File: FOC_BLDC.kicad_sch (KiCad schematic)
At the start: 0 parts

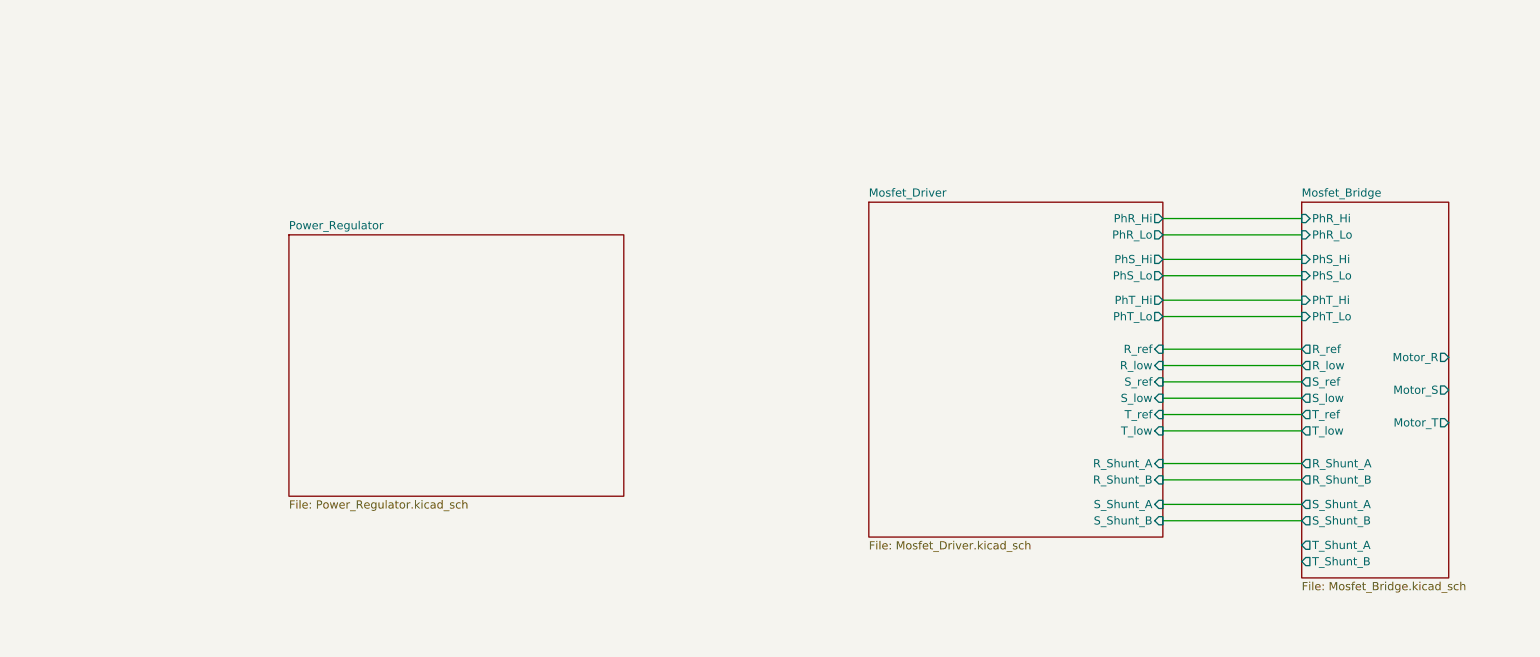
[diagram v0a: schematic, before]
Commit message: Finished basic schematic.
Need to add inline opamps and footprints to all components.
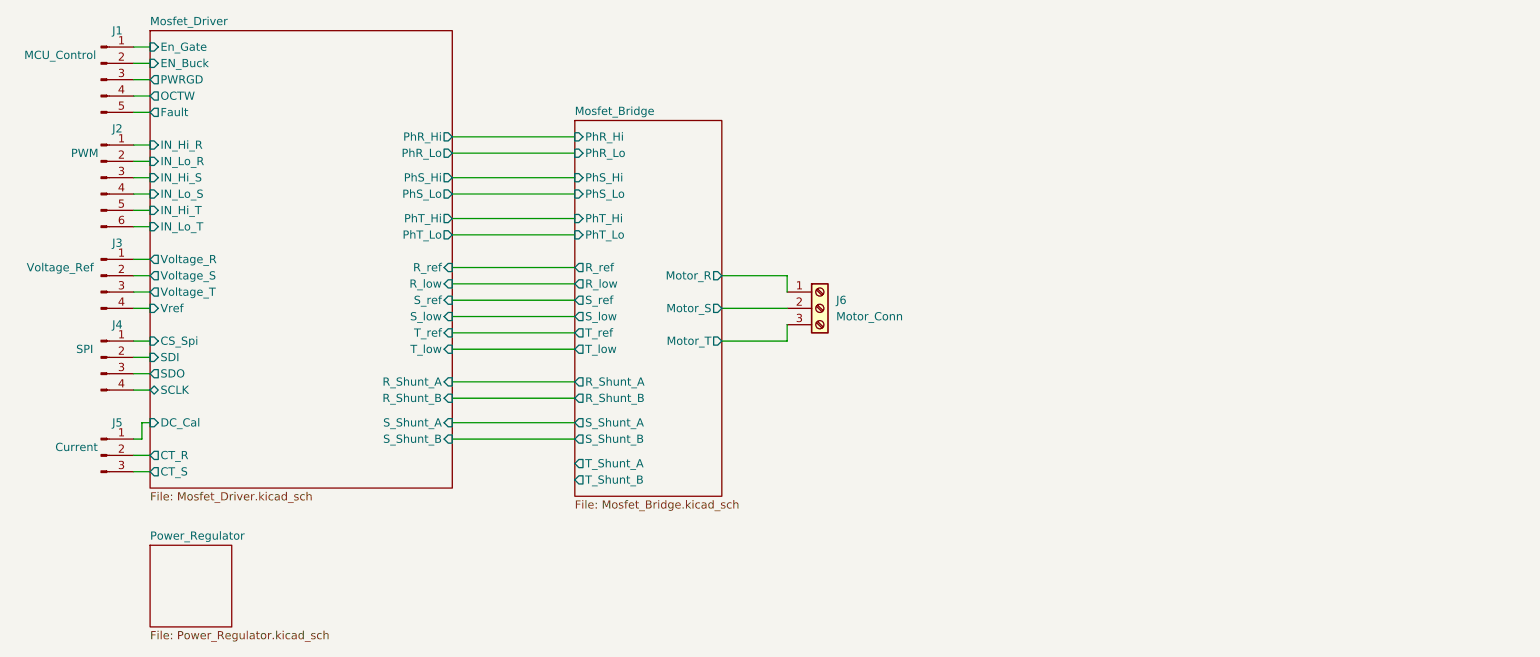
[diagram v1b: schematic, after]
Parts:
- added J1: MCU_Control, Connector_PinHeader_2.54mm:PinHeader_1x05_P2.54mm_Vertical, symbol Connector:Conn_01x05_Male
- added J2: PWM, symbol Connector:Conn_01x06_Male
- added J3: Voltage_Ref, Connector_PinHeader_2.54mm:PinHeader_1x04_P2.54mm_Vertical, symbol Connector:Conn_01x04_Male
- added J4: SPI, Connector_PinHeader_2.54mm:PinHeader_1x04_P2.54mm_Vertical, symbol Connector:Conn_01x04_Male
- added J5: Current, Connector_PinHeader_2.54mm:PinHeader_1x03_P2.54mm_Vertical, symbol Connector:Conn_01x03_Male
- added J6: Motor_Conn, symbol Connector:Screw_Terminal_01x03
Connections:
- net Mosfet_Bridge/Motor_R: now also J6.1 (Pin_1)
- net Mosfet_Bridge/Motor_S: now also J6.2 (Pin_2)
- net Mosfet_Bridge/Motor_T: now also J6.3 (Pin_3)
- new net Mosfet_Driver/CS_Spi: J4.1 (Pin_1)
- new net Mosfet_Driver/CT_R: J5.2 (Pin_2)
- new net Mosfet_Driver/CT_S: J5.3 (Pin_3)
- new net Mosfet_Driver/DC_Cal: J5.1 (Pin_1)
- new net Mosfet_Driver/EN_Buck: J1.2 (Pin_2)
- new net Mosfet_Driver/En_Gate: J1.1 (Pin_1)
- new net Mosfet_Driver/Fault: J1.5 (Pin_5)
- new net Mosfet_Driver/IN_Hi_R: J2.1 (Pin_1)
- new net Mosfet_Driver/IN_Hi_S: J2.3 (Pin_3)
- new net Mosfet_Driver/IN_Hi_T: J2.5 (Pin_5)
- new net Mosfet_Driver/IN_Lo_R: J2.2 (Pin_2)
- new net Mosfet_Driver/IN_Lo_S: J2.4 (Pin_4)
- new net Mosfet_Driver/IN_Lo_T: J2.6 (Pin_6)
- new net Mosfet_Driver/OCTW: J1.4 (Pin_4)
- new net Mosfet_Driver/PWRGD: J1.3 (Pin_3)
- new net Mosfet_Driver/SCLK: J4.4 (Pin_4)
- new net Mosfet_Driver/SDI: J4.2 (Pin_2)
- new net Mosfet_Driver/SDO: J4.3 (Pin_3)
- new net Mosfet_Driver/Voltage_R: J3.1 (Pin_1)
- new net Mosfet_Driver/Voltage_S: J3.2 (Pin_2)
- new net Mosfet_Driver/Voltage_T: J3.3 (Pin_3)
- new net Mosfet_Driver/Vref: J3.4 (Pin_4)
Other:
- sheet Mosfet_Driver ports: added CS_Spi, CT_R, CT_S, DC_Cal, EN_Buck, En_Gate, Fault, IN_Hi_R, IN_Hi_S, IN_Hi_T, IN_Lo_R, IN_Lo_S, IN_Lo_T, OCTW, PWRGD, SCLK, SDI, SDO, Voltage_R, Voltage_S, Voltage_T, Vref; removed none
